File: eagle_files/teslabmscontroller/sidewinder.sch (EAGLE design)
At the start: 42 parts, among them J1 TERMINAL12, J2 TERMINAL12, Q1 2N3704, Q2 2N3906, T1 V_REG_317SINK, U1 G3VM41, U2 G3VM41, U3 G3VM41, U4 SN65HVD230, U5 SP720APP, U6 SP720APP

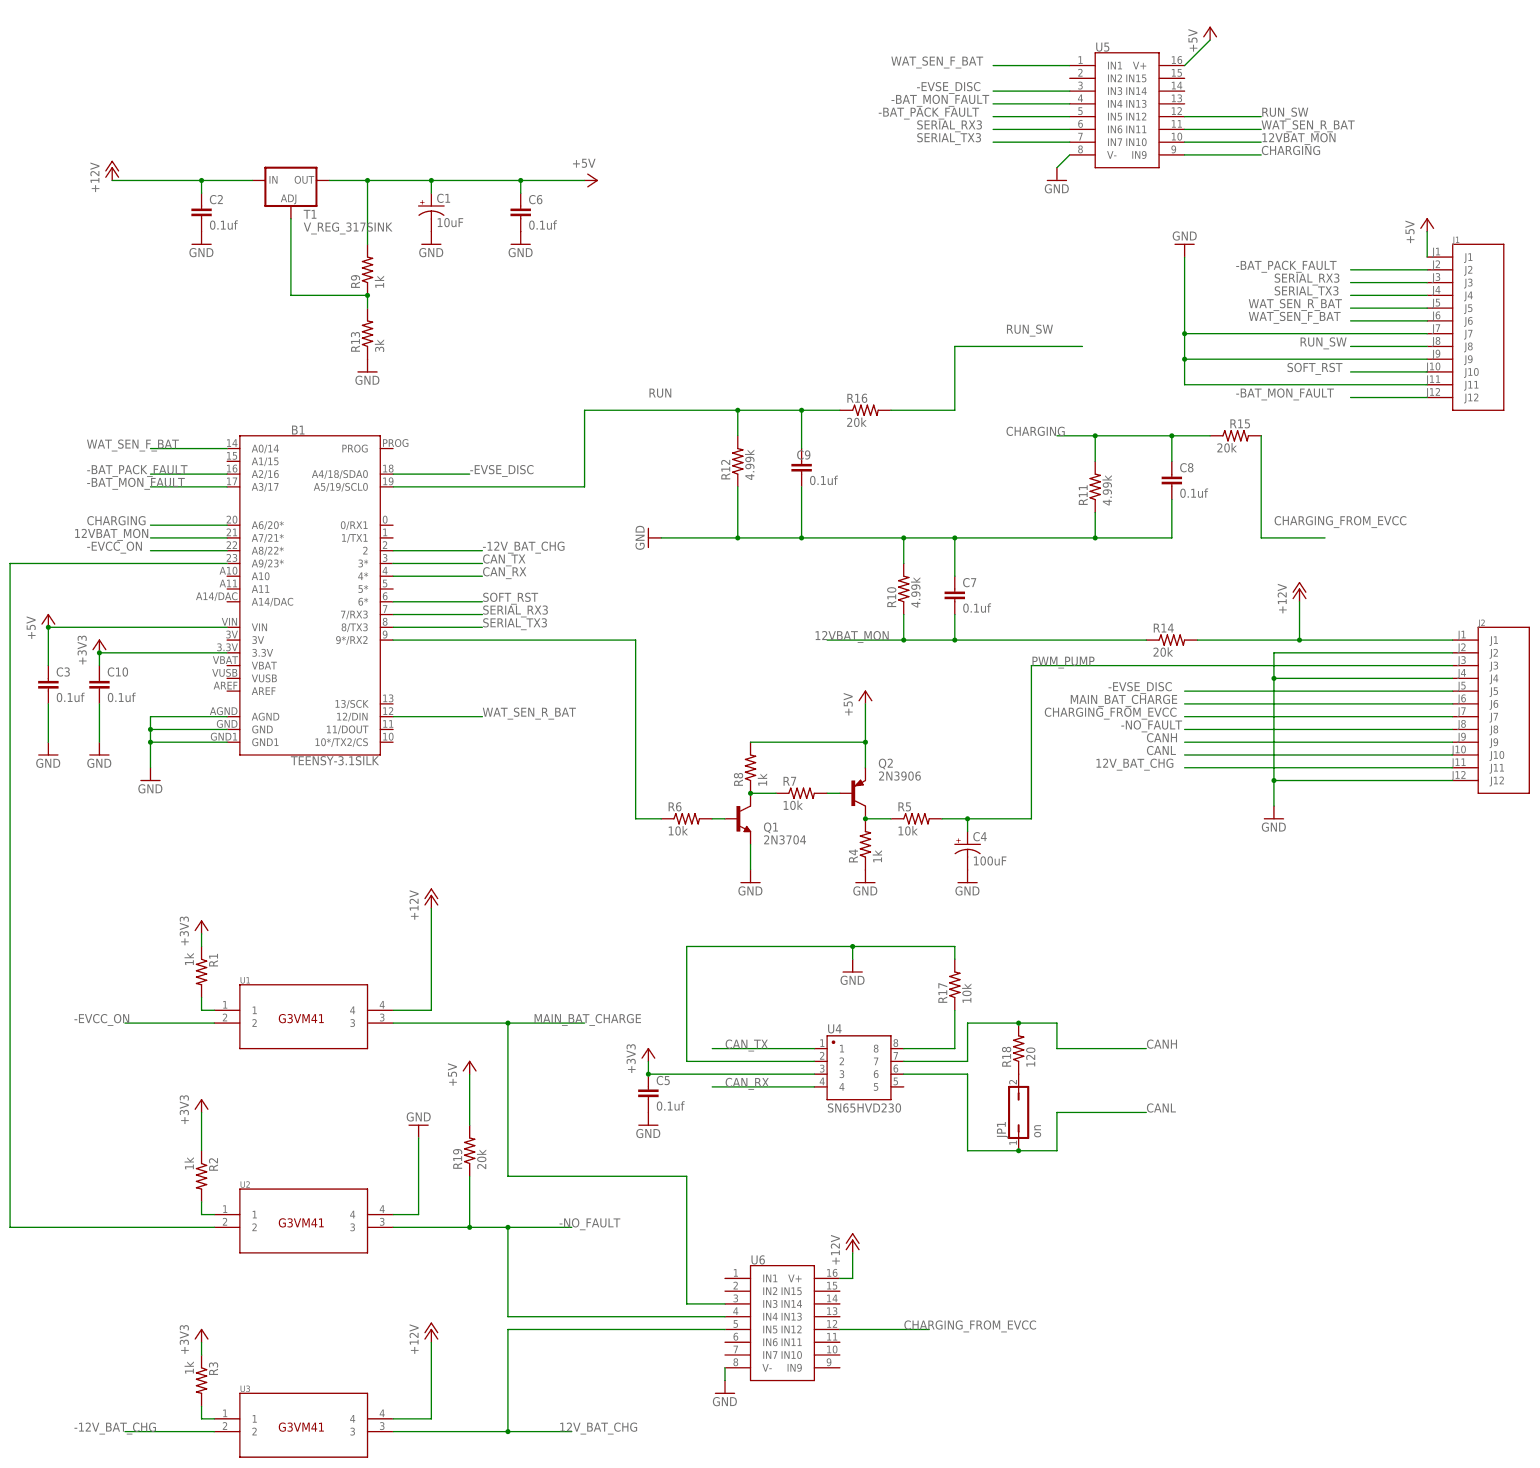
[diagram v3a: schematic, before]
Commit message: updated BMS board
fixed can bus chip and changed 5v regulator to a switching to avoid heat.
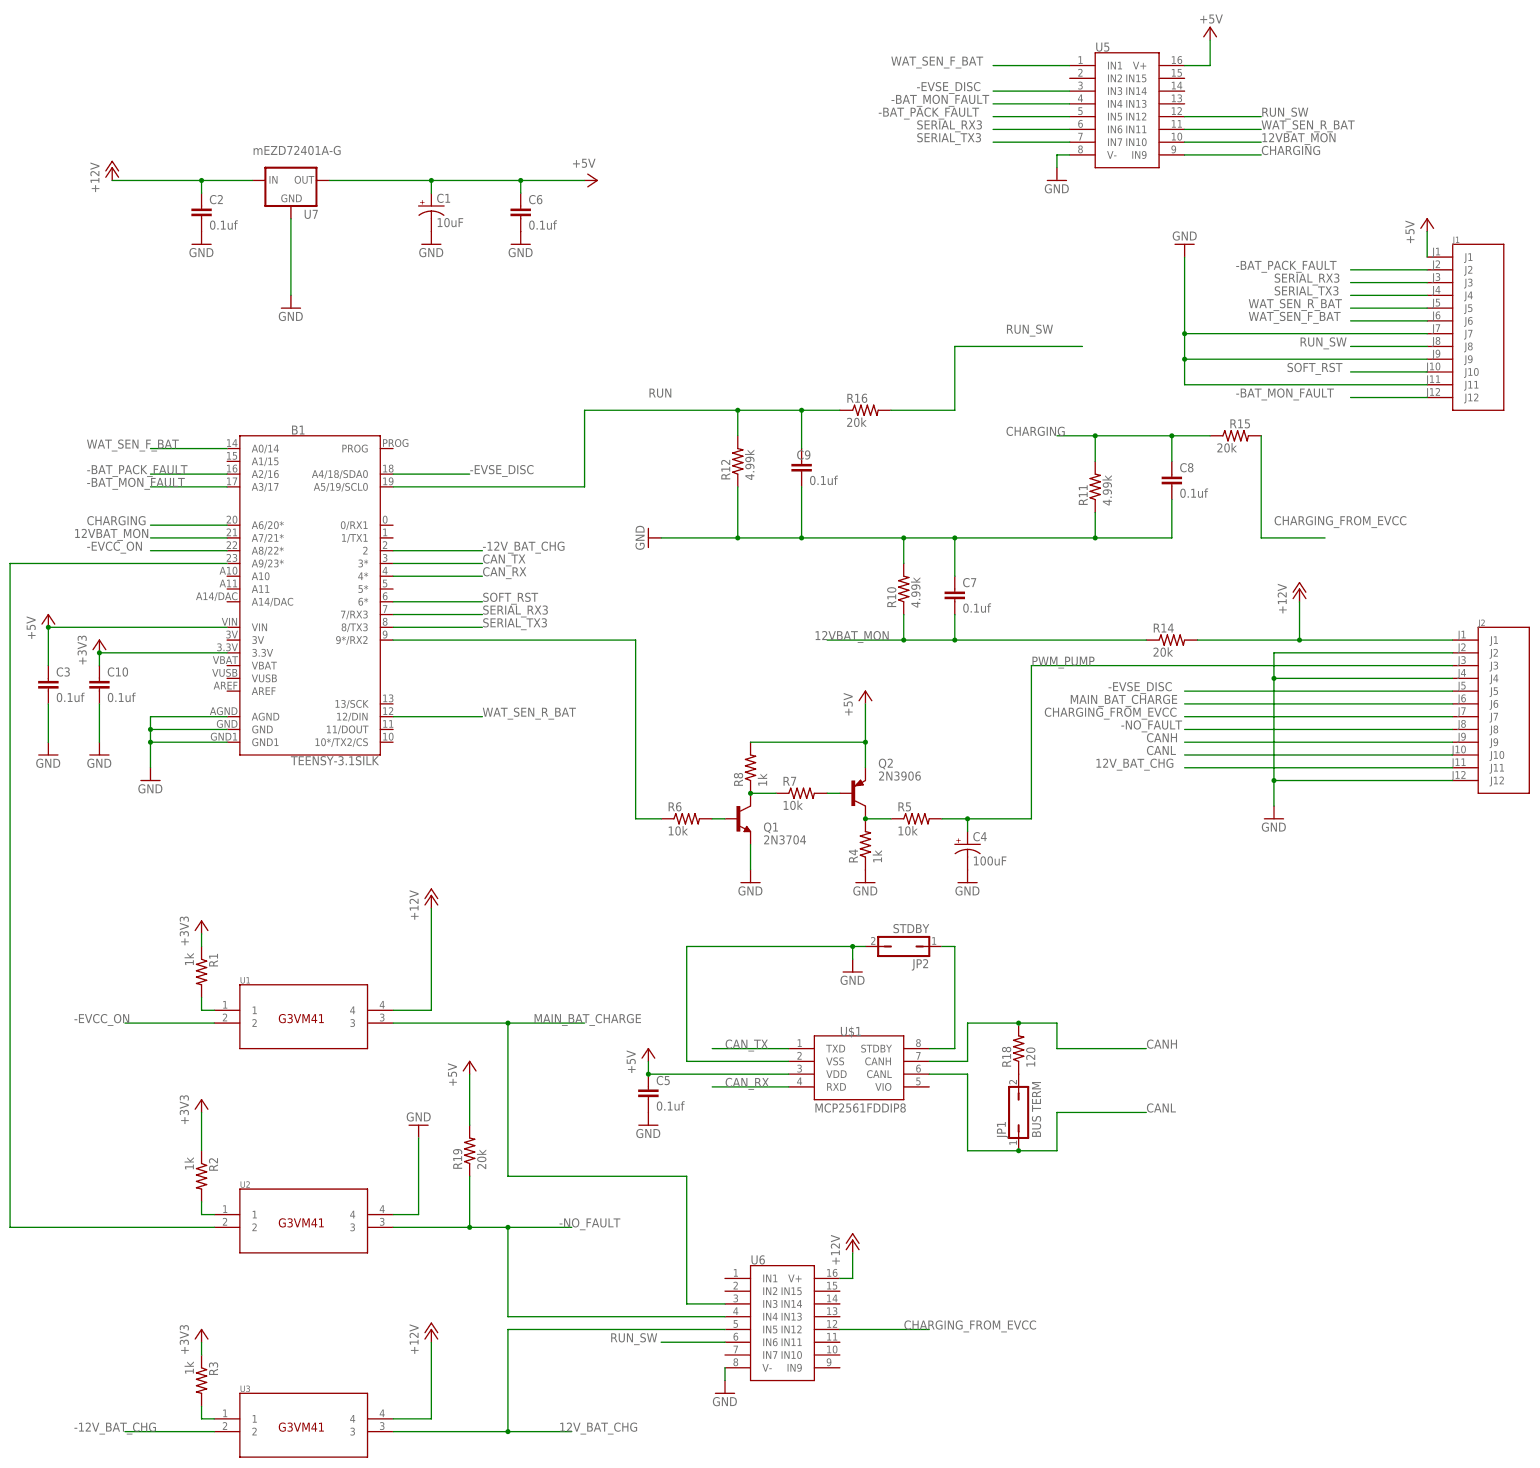
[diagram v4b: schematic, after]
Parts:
- removed R13: 3k, rcl:R-US_0207/10
- removed R17: 10k, rcl:R-US_0207/10
- removed R9: 1k, rcl:R-US_0207/10
- removed T1: V_REG_317SINK, SparkFun-IC-Power:V_REG_317SINK
- removed U4: SN65HVD230, SparkFun-Retired:GENERIC-SOIC8MSGEQ7N-FILTER
- added JP2: STDBY, jumper:JP1Q
- added U$1: MCP2561FDDIP8, MCP2561FD:MCP2561FDDIP8
- added U7: mEZD72401A-G, SparkFun-IC-Power:V_REG_78XXSINK
- JP1: value on -> BUS TERM
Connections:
- removed net N$15: R13.2, R9.1, T1.ADJ
- net +12V: now also U7.IN; no longer T1.IN
- net +3V3: no longer C5.1, U4.3
- net +5V: now also C5.1, U$1.VDD, U7.OUT; no longer R9.2, T1.OUT
- net CANH: now also U$1.CANH; no longer U4.7
- net CANL: now also U$1.CANL; no longer U4.6
- net CAN_RX: now also U$1.RXD; no longer U4.4
- net CAN_TX: now also U$1.TXD; no longer U4.1
- net GND: now also JP2.2, U$1.VSS, U7.GND; no longer R13.1, R17.2, U4.2
- net N$12: now also JP2.1, U$1.STDBY; no longer R17.1, U4.8
- net RUN_SW: now also U6.IN6

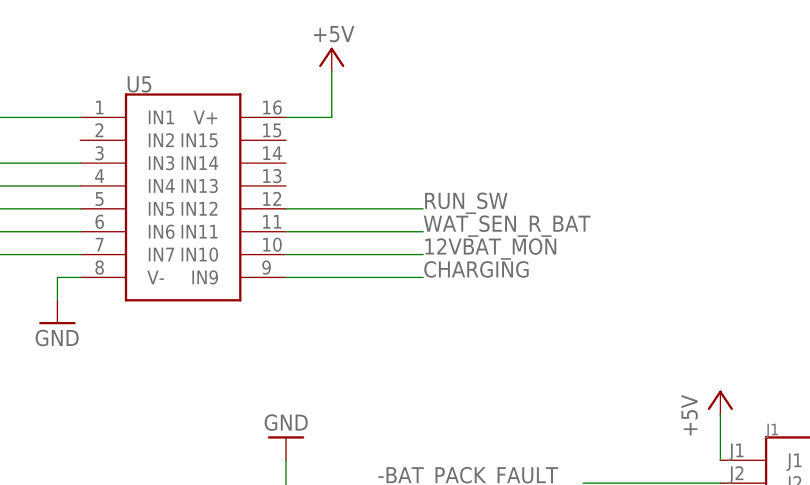
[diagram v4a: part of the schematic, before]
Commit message: fixed CAN
Fixed can bus
fixed bug on PCB where run input was connected to both 5v and 12v chips.
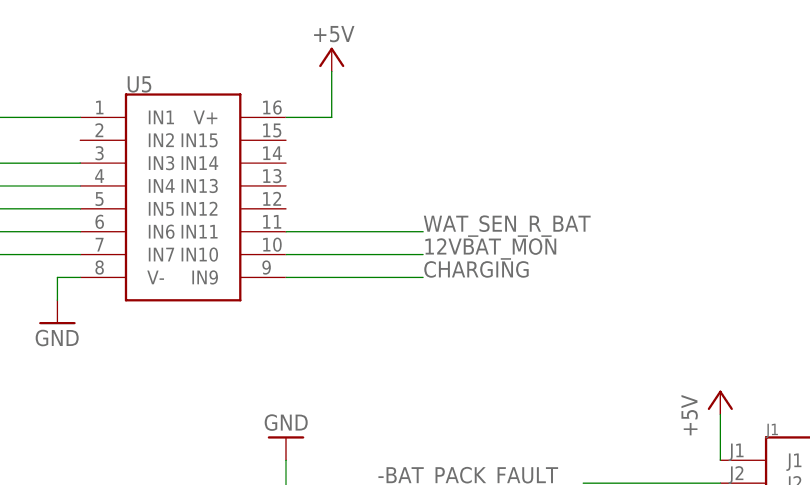
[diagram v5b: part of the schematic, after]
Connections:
- net RUN_SW: no longer U5.IN12
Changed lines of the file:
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@@
-</segment>
-<segment>
-<pinref part="U5" gate="G$1" pin="IN12"/>
-<wire x1="208.28" y1="154.94" x2="223.52" y2="154.94" width="0.1524" layer="91"/>
-<label x="223.52" y="154.94" size="1.778" layer="95"/>
 </segment>
 <segment>
